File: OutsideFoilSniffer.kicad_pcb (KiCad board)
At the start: 2 copper layers, 85.1 x 105.4 mm, 40 parts, among them J1 Black, J2 Red, J3 Signal, J4 Conn_01x15_Male, J5 Conn_01x15_Male, K1 SANYOU_SRD_Form_C, Q1 BC547, Q2 2N3904

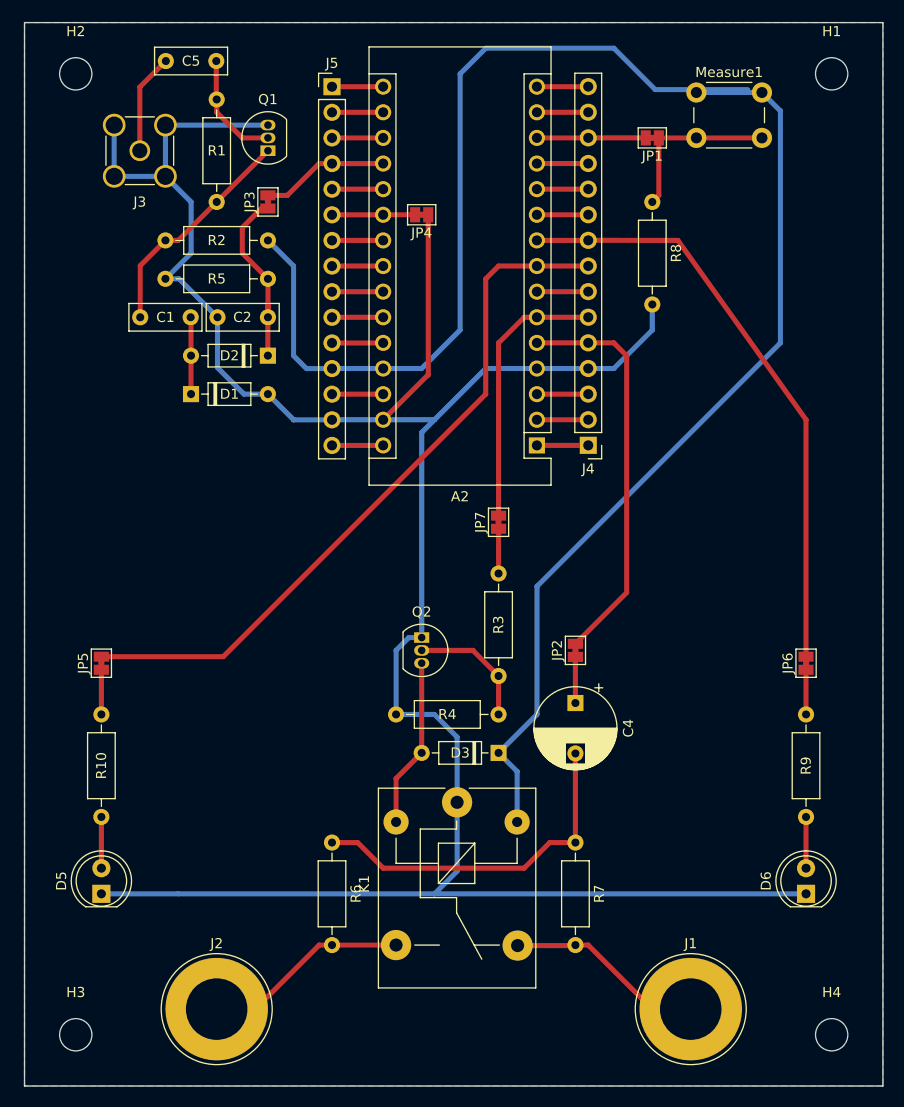
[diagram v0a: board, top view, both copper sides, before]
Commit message: Modified size to fit PCBWay prototype size 100x80 mm for cheap price
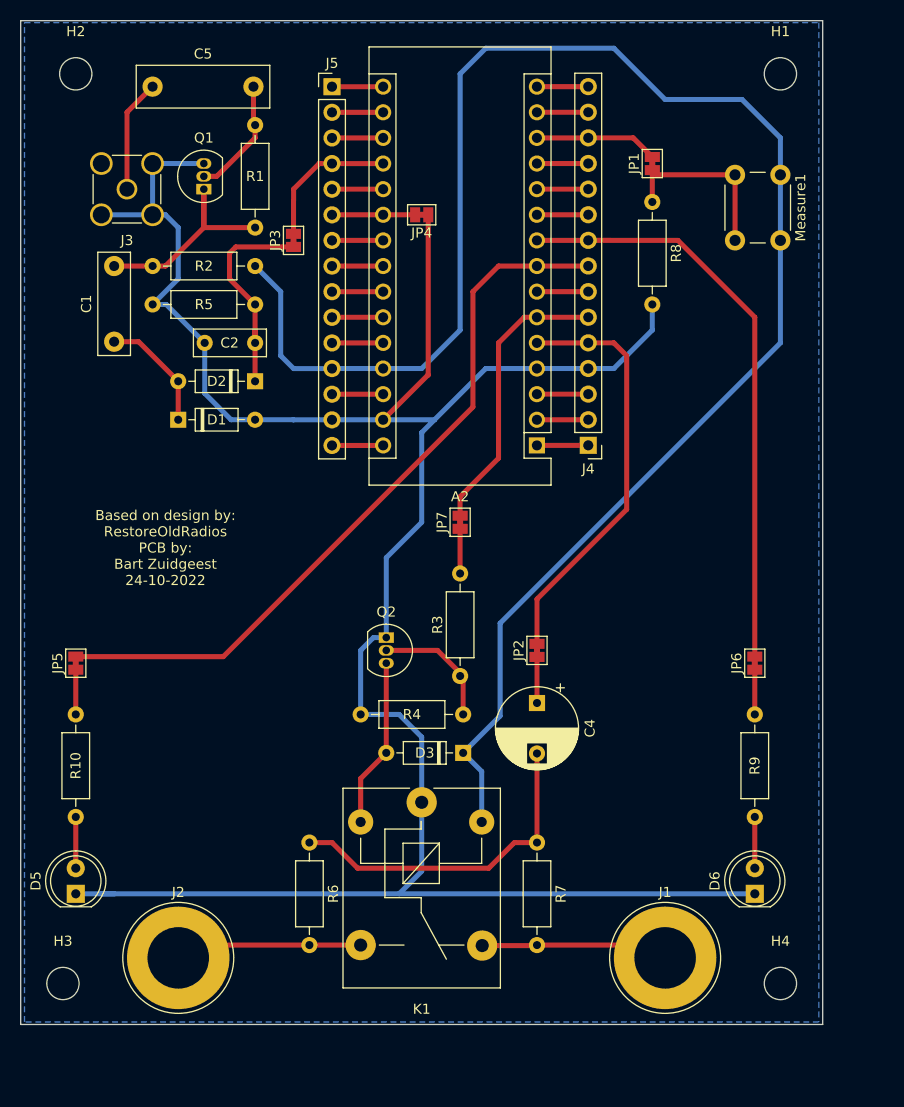
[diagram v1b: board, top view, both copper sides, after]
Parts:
- C1: footprint Capacitor_THT:C_Rect_L7.0mm_W2.5mm_P5.00mm -> Capacitor_THT:C_Rect_L10.0mm_W3.0mm_P7.50mm_MKS4
- C5: footprint Capacitor_THT:C_Rect_L7.0mm_W2.5mm_P5.00mm -> Capacitor_THT:C_Rect_L13.0mm_W4.0mm_P10.00mm_FKS3_FKP3_MKS4
- moved Measure1 11.7 mm to (130.8, 74.8), turned to -90 degrees
- moved C1 7.96 mm to (64.8, 91.3), turned to 90 degrees
- moved Q1 7.41 mm to (73.7, 76.2)
- moved H4 7.18 mm to (130.8, 154.9)
- moved J2 6.35 mm to (71.1, 152.4)
- moved J1 5.68 mm to (119.4, 152.4)
- moved H3 5.24 mm to (59.7, 154.9)
- moved D6 5.08 mm to (128.3, 146.1)
- moved H1 5.08 mm to (130.8, 64.8)
- moved JP6 5.08 mm to (128.3, 123.2)
- moved R9 5.08 mm to (128.3, 128.3)
- moved R1 4.58 mm to (78.7, 80.0)
- moved JP3 4.58 mm to (82.5, 81.3)
- moved J3 4.02 mm to (66.0, 76.2)
- moved JP7 3.81 mm to (99.1, 109.2)
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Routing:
- net PINGND: track 247.9 -> 237.6 mm
- net PIN27: track 179.7 -> 173.3 mm
- net Net-(C1-Pad1): track 7.66 -> 11.8 mm
- net Net-(C2-Pad1): track 19.6 -> 22.9 mm
- net Net-(J1-Pad1): track 16.0 -> 18.9 mm
- net PIN8: track 71.0 -> 73.5 mm
- net Net-(J2-Pad1): track 16.6 -> 18.6 mm
- net Net-(JP1-Pad1): track 16.2 -> 18.1 mm
- net PIN19: track 12.7 -> 14.4 mm
- net PIN6: track 27.1 -> 28.7 mm
- net PIN5: track 40.1 -> 41.7 mm
- net PIN13: track 10.8 -> 12.2 mm
- net Net-(C4-Pad2): track 35.1 -> 33.8 mm
- net Net-(C5-Pad1): track 9.96 -> 11.2 mm
- net PIN9: track 59.3 -> 58.4 mm
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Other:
- board size 85.1 x 105.4 mm -> 79.5 x 99.5 mm
- board text added: "Based on design by: RestoreOldRadios PCB by: Bart Zuidgeest 24-10-2022"
